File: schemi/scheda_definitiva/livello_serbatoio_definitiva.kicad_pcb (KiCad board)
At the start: 2 copper layers, 83 x 72 mm, 41 parts, among them J1 USB_B, J2 BTN_LED_GROUP, J3 CONN_LCD, J4 CONN_US, J5 ICSP, SW1 SW_RST, U1 FT232RL, U2 ATmega328P-PU, U3 USBLC6-2SC6, Y1 16MHz

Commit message: revisione routing pcb
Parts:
- moved R2 0.54 mm to (110.6, 90.9)
- moved R1 0.54 mm to (110.6, 94.9)
- moved J2 0.24 mm to (142.2, 135.4)
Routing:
- net Net-(D2-Pad1): track 30.2 -> 18.8 mm
- net VDD: track 256.0 -> 246.2 mm
- net Net-(D1-Pad1): track 27.8 -> 25.9 mm
- net D_IN_-: track 8.44 -> 9.59 mm
- net Net-(R1-Pad2): track 22.4 -> 21.4 mm
- net D_IN_+: track 9.87 -> 10.8 mm
- net /X1: track 16.8 -> 17.8 mm
- net /X2: track 16.6 -> 17.6 mm
- net Net-(D1-Pad2): track 20.3 -> 19.7 mm
- net DTR: track 84.8 -> 85.4 mm
- net Net-(D4-Pad2): track 22.4 -> 23.0 mm
- net Net-(R2-Pad2): track 20.3 -> 20.9 mm

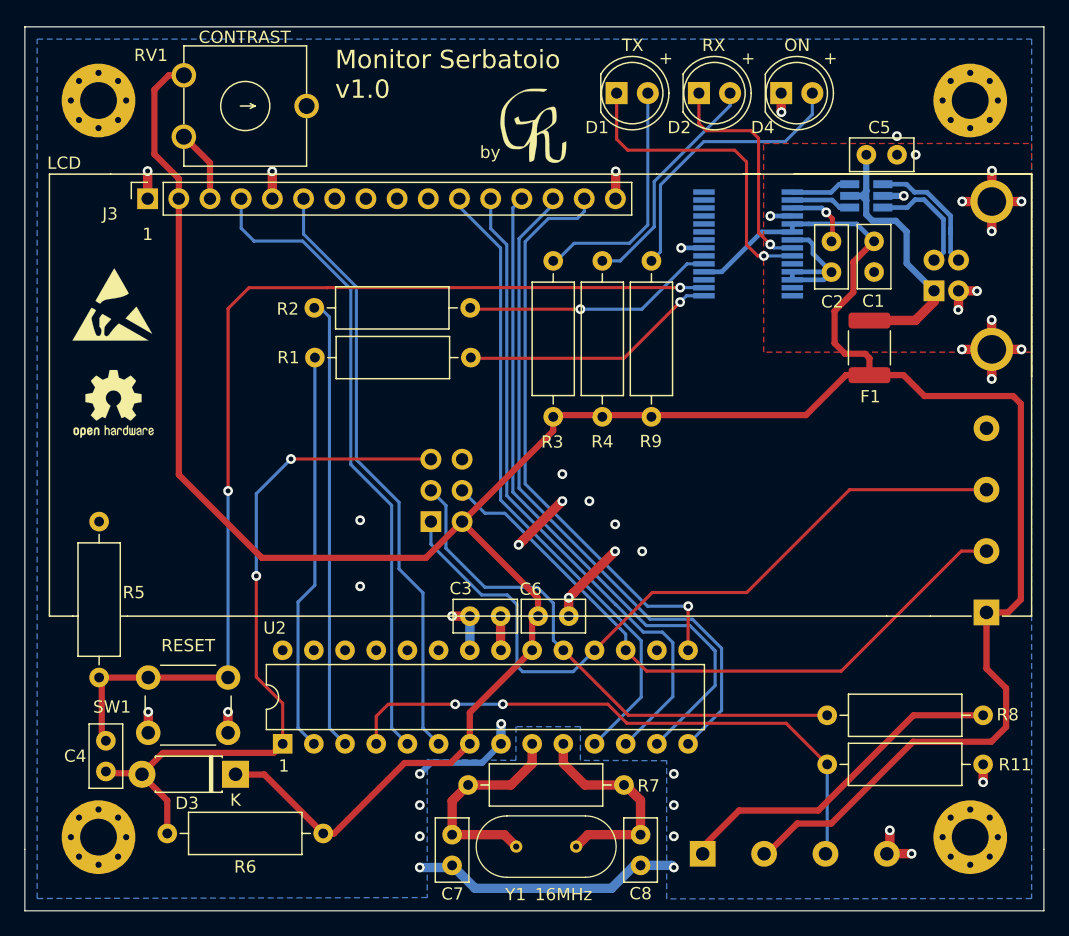
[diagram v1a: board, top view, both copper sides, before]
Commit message: esportati pin per espandibilità
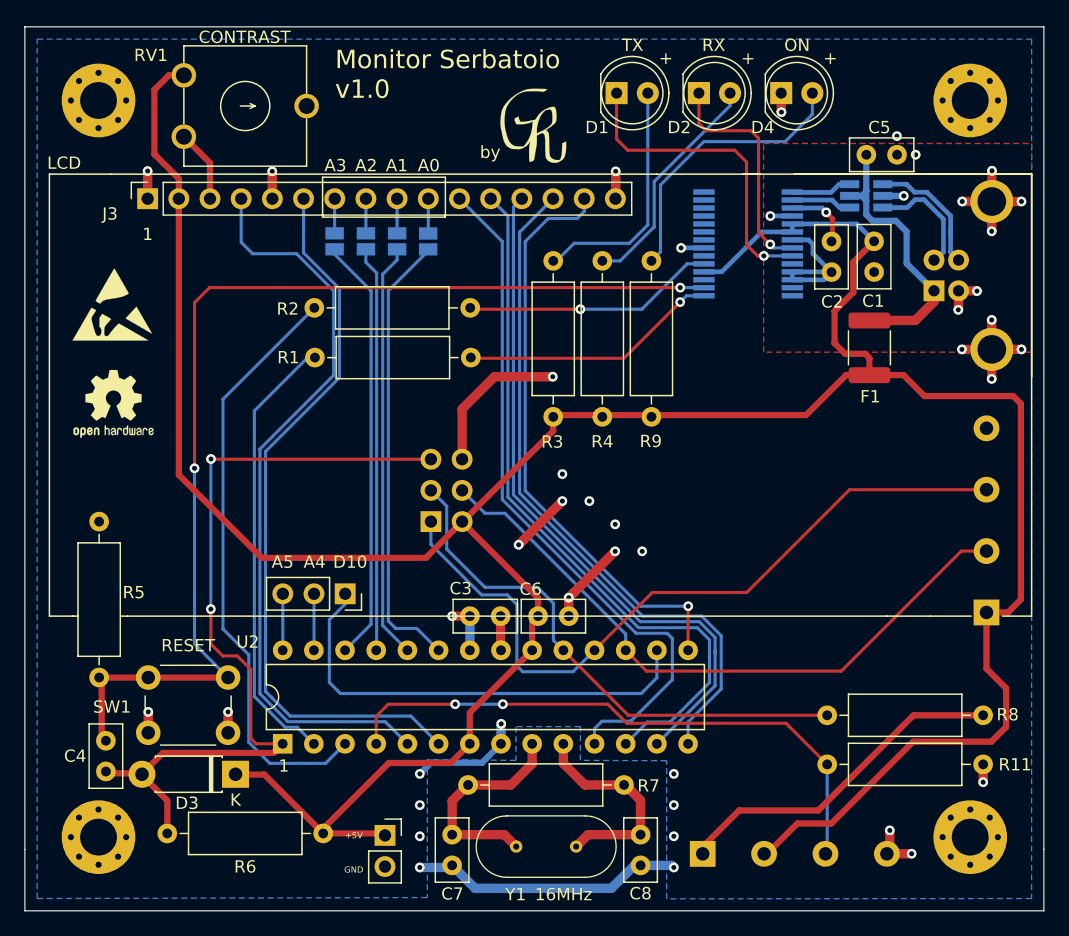
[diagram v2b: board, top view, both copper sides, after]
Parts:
- added J7: Exp_Analog, Connector_PinSocket_2.54mm:PinSocket_1x03_P2.54mm_Vertical, F.Cu at (113.1, 114.2)
- added J8: Exp_Alim, Connector_PinSocket_2.54mm:PinSocket_1x02_P2.54mm_Vertical, F.Cu at (116.3, 133.9)
- added JP1: A0J, Jumper:SolderJumper-2_P1.3mm_Open_Pad1.0x1.5mm, B.Cu at (112.2, 85.5)
- added JP2: A1J, Jumper:SolderJumper-2_P1.3mm_Open_Pad1.0x1.5mm, B.Cu at (114.8, 85.5)
- added JP3: A2J, Jumper:SolderJumper-2_P1.3mm_Open_Pad1.0x1.5mm, B.Cu at (117.3, 85.5)
- added JP4: A3J, Jumper:SolderJumper-2_P1.3mm_Open_Pad1.0x1.5mm, B.Cu at (119.8, 85.5)
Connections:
- U2 pad 16: Net-(U2-Pad16) -> D10
- U2 pad 23: Net-(U2-Pad23) -> A0
- U2 pad 24: Net-(U2-Pad24) -> A1
- U2 pad 25: Net-(U2-Pad25) -> A2
- U2 pad 26: Net-(U2-Pad26) -> A3
- U2 pad 27: Net-(U2-Pad27) -> A4
- U2 pad 28: Net-(U2-Pad28) -> A5
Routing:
- net D10: track 0.00 -> 37.6 mm
- net A0: track 0.00 -> 36.9 mm
- net A3: track 0.00 -> 34.8 mm
- net A1: track 0.00 -> 34.0 mm
- net A2: track 0.00 -> 33.0 mm
- net GND: track 104.4 -> 117.0 mm, vias 44 -> 43
- net RX: track 37.1 -> 48.5 mm
- net D4: track 49.0 -> 59.7 mm
- net D3: track 52.3 -> 61.7 mm
- net ICSP_RST: track 57.9 -> 66.7 mm
- net D6: track 53.1 -> 58.5 mm
- net VDD: track 246.2 -> 251.6 mm
- net D5: track 52.1 -> 57.1 mm
- net A5: track 0.00 -> 4.60 mm
- net A4: track 0.00 -> 4.60 mm
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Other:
- board text added: "A0"
- board text added: "A1"
- board text added: "A2"
- board text added: "A3"
- board text added: "A4"
- board text added: "A5"
- board text added: "D10"

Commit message: revisioni minime a pcb
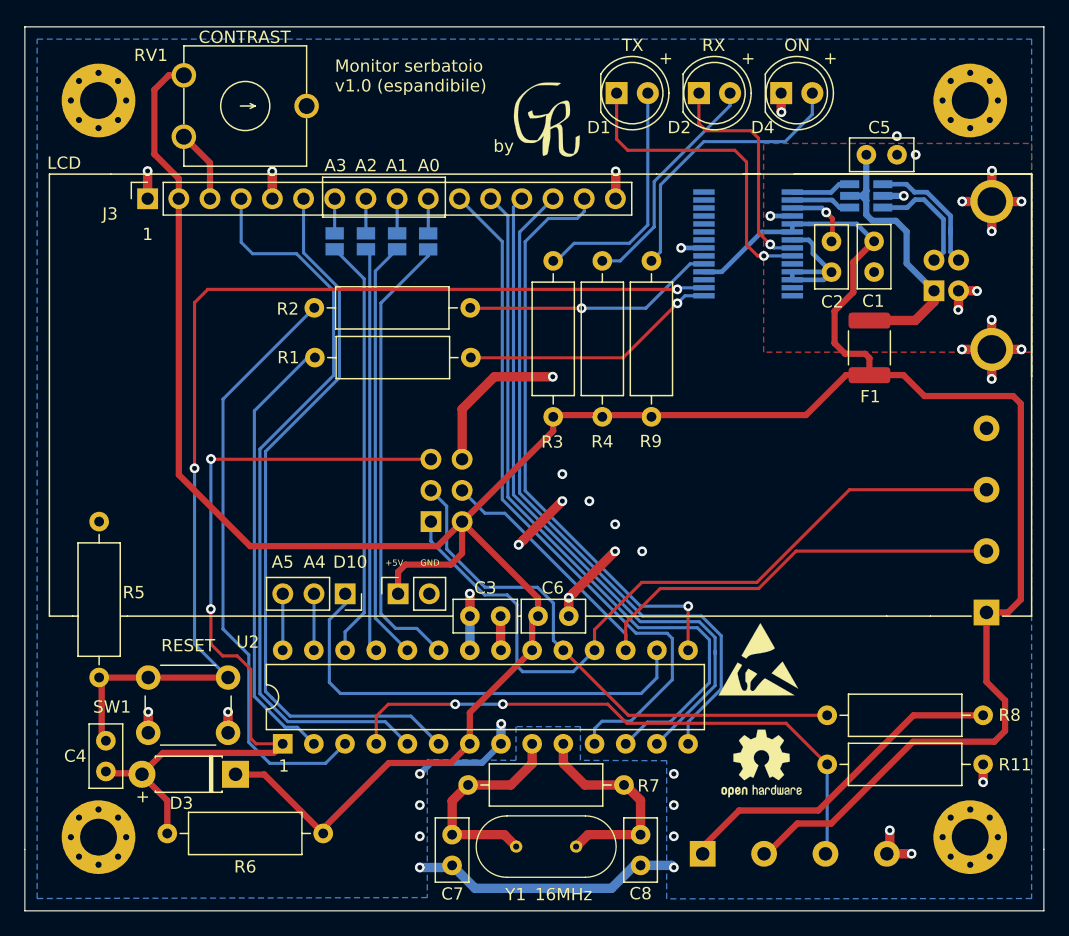
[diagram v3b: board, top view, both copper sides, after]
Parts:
- moved REF** 60.4 mm to (147.0, 128.0)
- moved REF** 60.0 mm to (146.8, 119.5)
- moved J8 19.7 mm to (117.4, 114.2), turned to 90 degrees
- moved G*** 1.21 mm to (129.5, 75.6)
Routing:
- net VDD: track 251.6 -> 256.0 mm
- net D12: track 60.5 -> 61.3 mm
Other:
- board text added: "Monitor serbatoio v1.0 (espandibile)"
- board text removed: "Monitor Serbatoio v1.0"

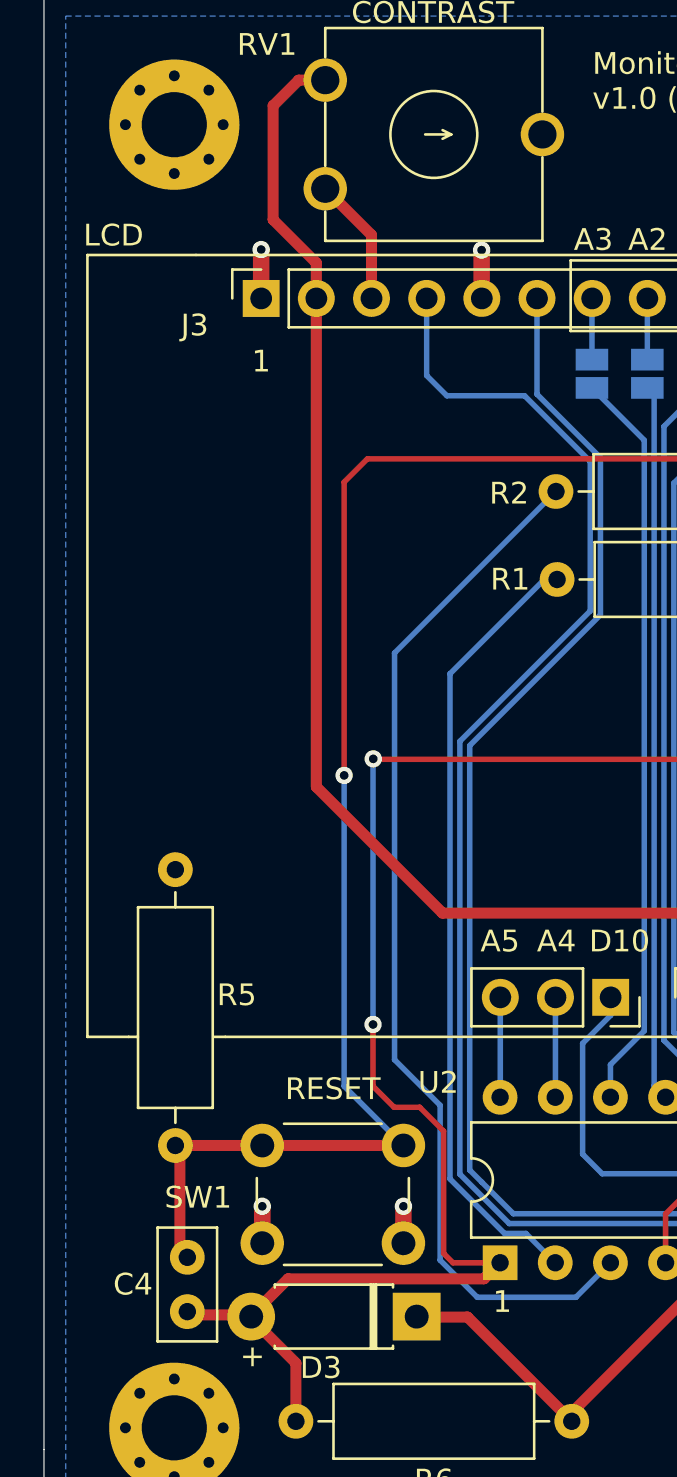
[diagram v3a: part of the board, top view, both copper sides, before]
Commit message: fix footprint trimmer - aggiornato pcb
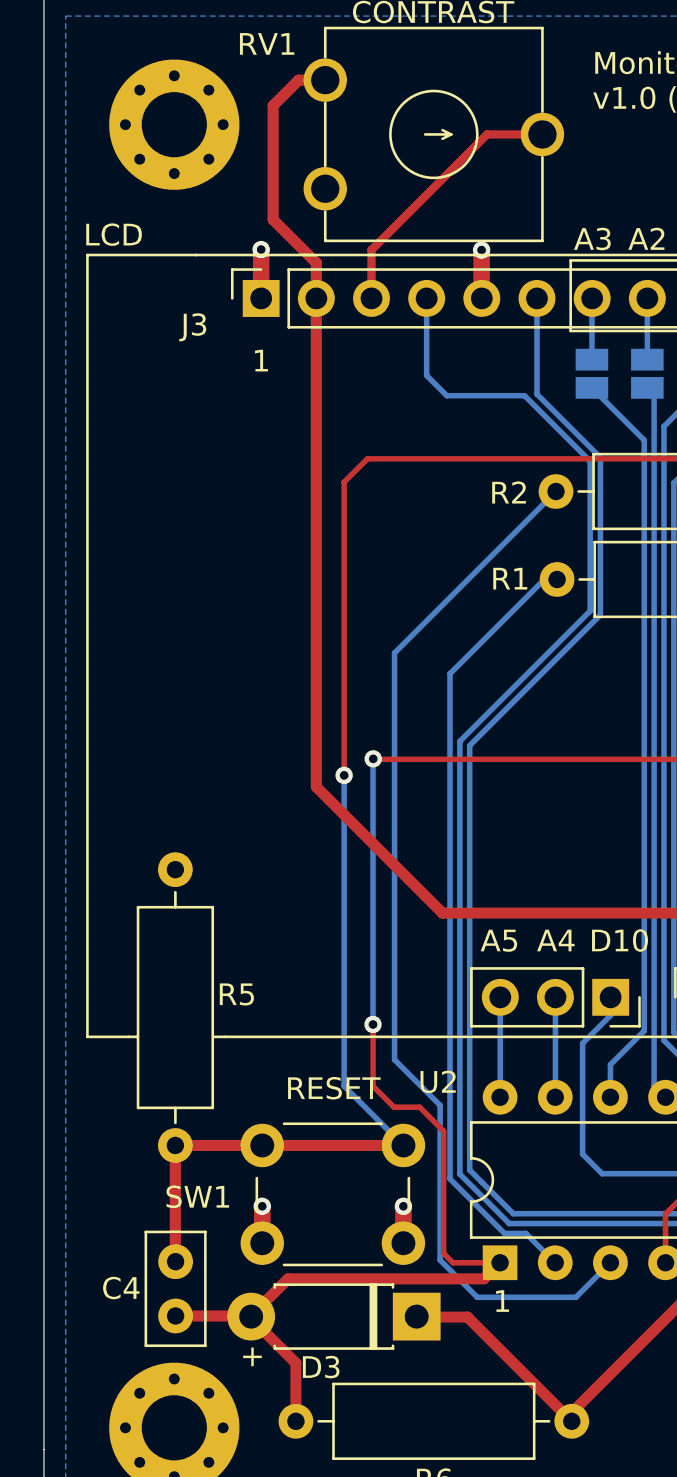
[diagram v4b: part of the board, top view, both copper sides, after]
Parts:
- moved C4 0.58 mm to (93.1, 128.8)
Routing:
- net V0: track 5.93 -> 12.3 mm
- net ICSP_RST: track 66.7 -> 67.4 mm

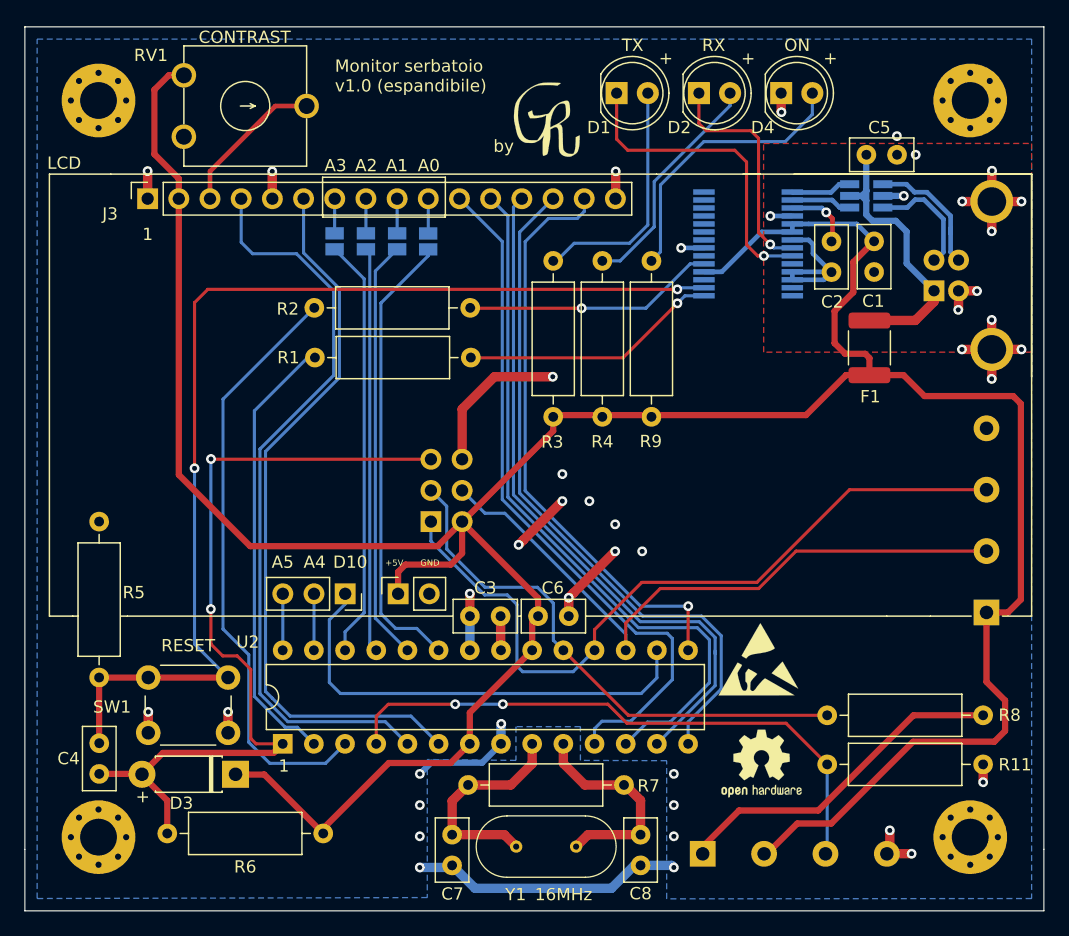
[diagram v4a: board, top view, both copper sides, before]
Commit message: aggiornamento PCB - ridefinite filled zone - stondati bordi - cambiato connettore per espansione - rimosse via per GND
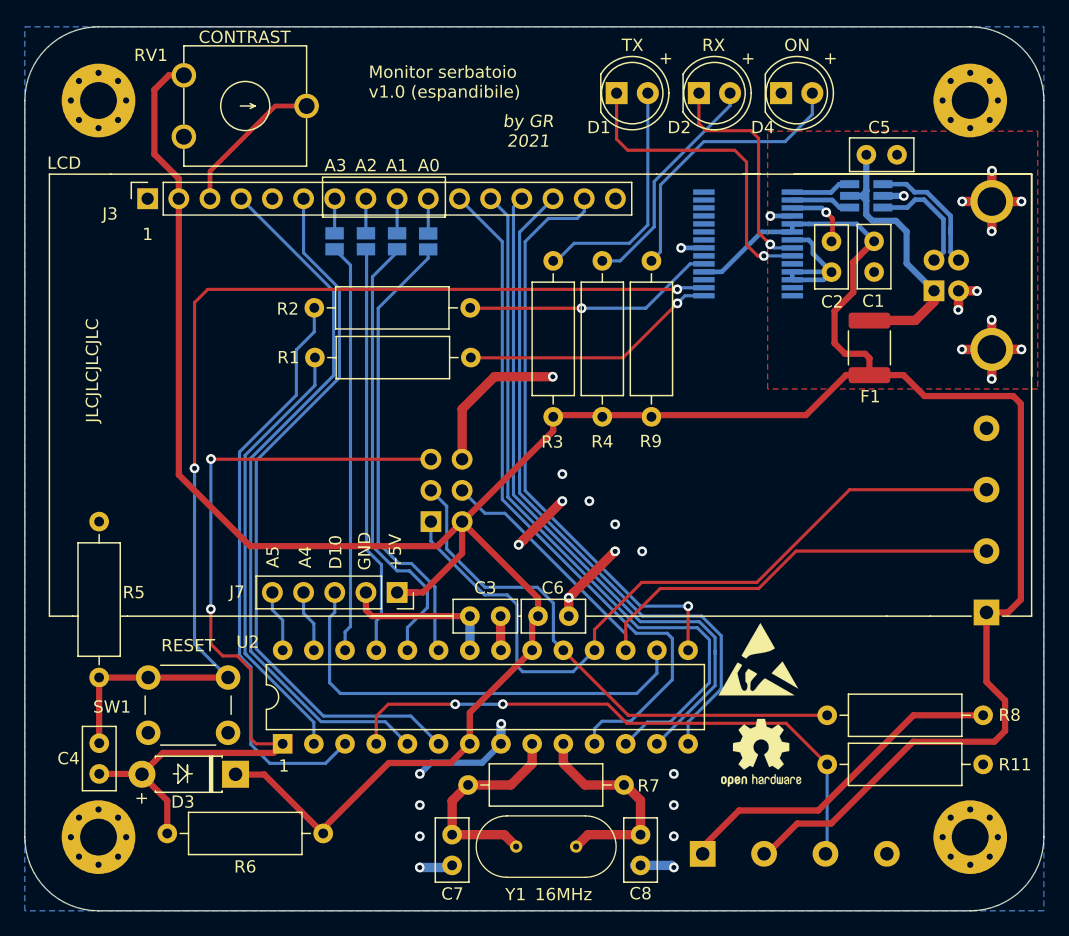
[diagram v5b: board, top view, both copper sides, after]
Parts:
- removed G***: LOGO, simboli_custom:logo
- removed J8: Exp_Alim, Connector_PinSocket_2.54mm:PinSocket_1x02_P2.54mm_Vertical
- J7: footprint Connector_PinSocket_2.54mm:PinSocket_1x03_P2.54mm_Vertical -> Connector_PinSocket_2.54mm:PinSocket_1x05_P2.54mm_Vertical
- moved J7 4.23 mm to (117.3, 114.1)
- moved REF** 0.87 mm to (147.0, 127.1)
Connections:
- J7 pad 1: D10 -> VDD
- J7 pad 2: A4 -> GND
- J7 pad 3: A5 -> D10
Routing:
- net GND: track 117.4 -> 92.5 mm, vias 43 -> 31
- net D3: track 61.7 -> 58.7 mm
- net A1: track 34.5 -> 36.6 mm
- net D4: track 59.7 -> 58.7 mm
- net RX: track 48.5 -> 47.6 mm
- net A3: track 34.3 -> 33.4 mm
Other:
- outline, holes or cut-outs redrawn
- board text added: "JLCJLCJLCJLC"
- board text added: "by GR 2021"
- board text added: "i piedini per l'estensione sono allineati verticalmente"
- board text removed: "by"

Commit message: piccole revisioni PCB - spostate alcune piste per maggiore copertura filled zone - rivisti alcuni parametri per manufacturing (dimensione scritte, S/N) - rimosse alcune vie e piste per piano GND inutili
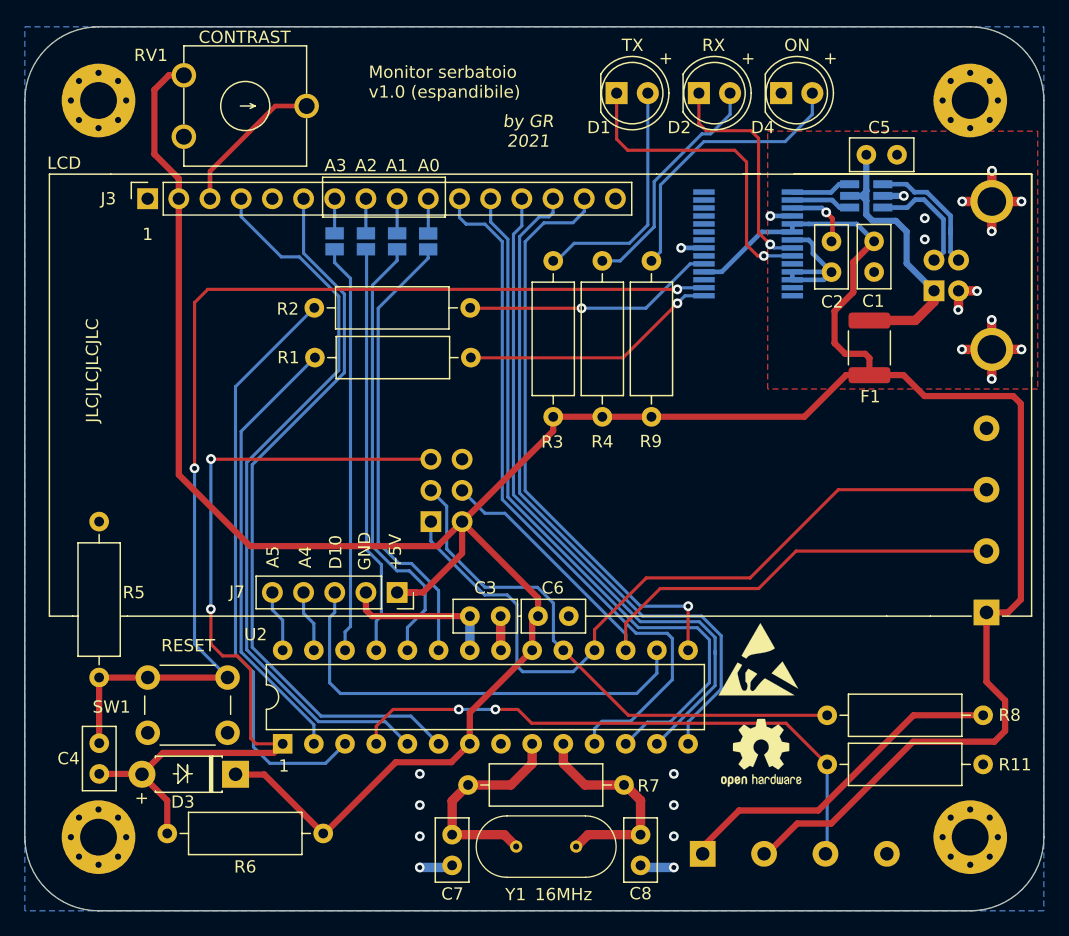
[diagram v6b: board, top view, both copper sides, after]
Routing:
- net GND: track 92.5 -> 58.3 mm, vias 31 -> 23
- net D3: track 58.7 -> 60.3 mm
- net D5: track 57.1 -> 58.0 mm
- net D2: track 48.9 -> 48.0 mm
- net D4: track 58.7 -> 59.5 mm
